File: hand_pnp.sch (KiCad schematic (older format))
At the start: 11 parts, among them J1 Solenoid, J2 Motor, J3 12v in, J4 AudioJack3_Ground, Q1 FDN339AN, Q2 FDN339AN, SW1 power sw

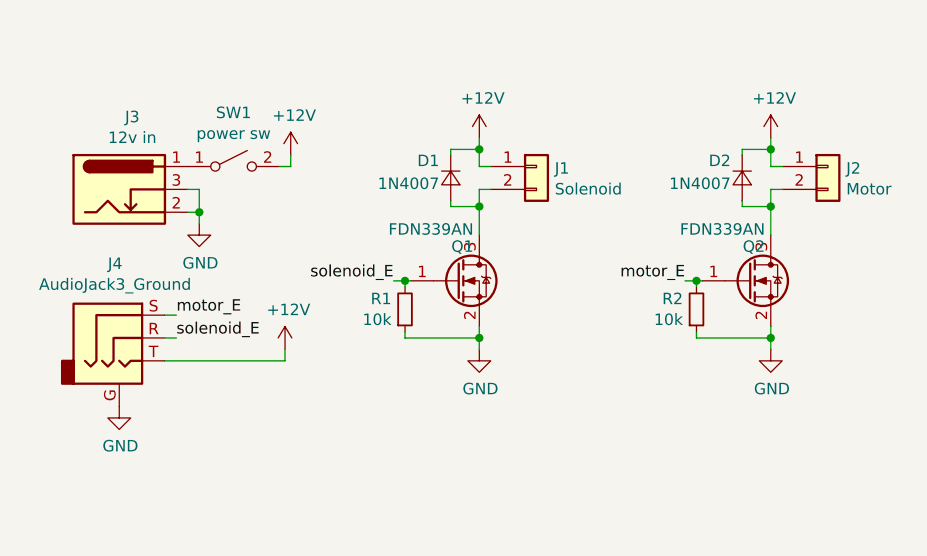
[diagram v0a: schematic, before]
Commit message: Modified board to make it smaller
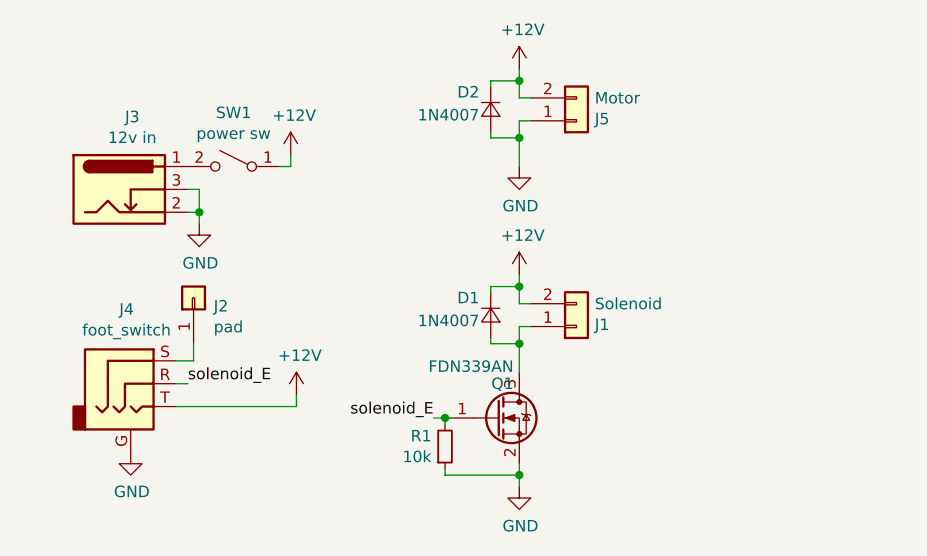
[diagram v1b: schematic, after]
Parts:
- removed J2: Motor, Connector_JST:JST_XH_S2B-XH-A_1x02_P2.50mm_Horizontal, symbol Connector_Generic:Conn_01x02
- removed Q2: FDN339AN, Package_TO_SOT_SMD:SOT-23_Handsoldering, symbol Device:Q_NMOS_GSD
- removed R2: 10k, Resistor_SMD:R_0603_1608Metric_Pad1.05x0.95mm_HandSolder, symbol Device:R_Small
- added J2: pad, TestPoint:TestPoint_THTPad_1.5x1.5mm_Drill0.7mm, symbol Connector_Generic:Conn_01x01
- added J5: Motor, Connector_PinHeader_2.54mm:PinHeader_1x02_P2.54mm_Vertical, symbol Connector_Generic:Conn_01x02
- J1, SW1: footprint Connector_JST:JST_XH_S2B-XH-A_1x02_P2.50mm_Horizontal -> Connector_PinHeader_2.54mm:PinHeader_1x02_P2.54mm_Horizontal
- J4: value AudioJack3_Ground -> foot_switch
- Q1: footprint Package_TO_SOT_SMD:SOT-23_Handsoldering -> Package_TO_SOT_SMD:SOT-23
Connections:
- net +12V: now also J1.2 (Pin_2), SW1.1 (A), J5.2 (Pin_2); no longer J1.1 (Pin_1), SW1.2 (B)
- net GND: now also D2.2 (A), J5.1 (Pin_1)
- net at D1.2 (A), Q1.3 (D): now also J1.1 (Pin_1); no longer J1.2 (Pin_2)
- net at J3.1: now also SW1.2 (B); no longer SW1.1 (A)
- net motor_E: no longer names the net of J4.S
- net motor_E: now also J2.1 (Pin_1)
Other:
- moved on the sheet: D1, J1, J4, Q1, R1
